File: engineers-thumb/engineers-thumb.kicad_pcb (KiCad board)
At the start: 2 copper layers, 19 parts, among them J1 Barrel_Jack_Switch, J2 AudioJack3_Switch, Q1 BC556, Q2 MMBFJ112, U1 ICL7660

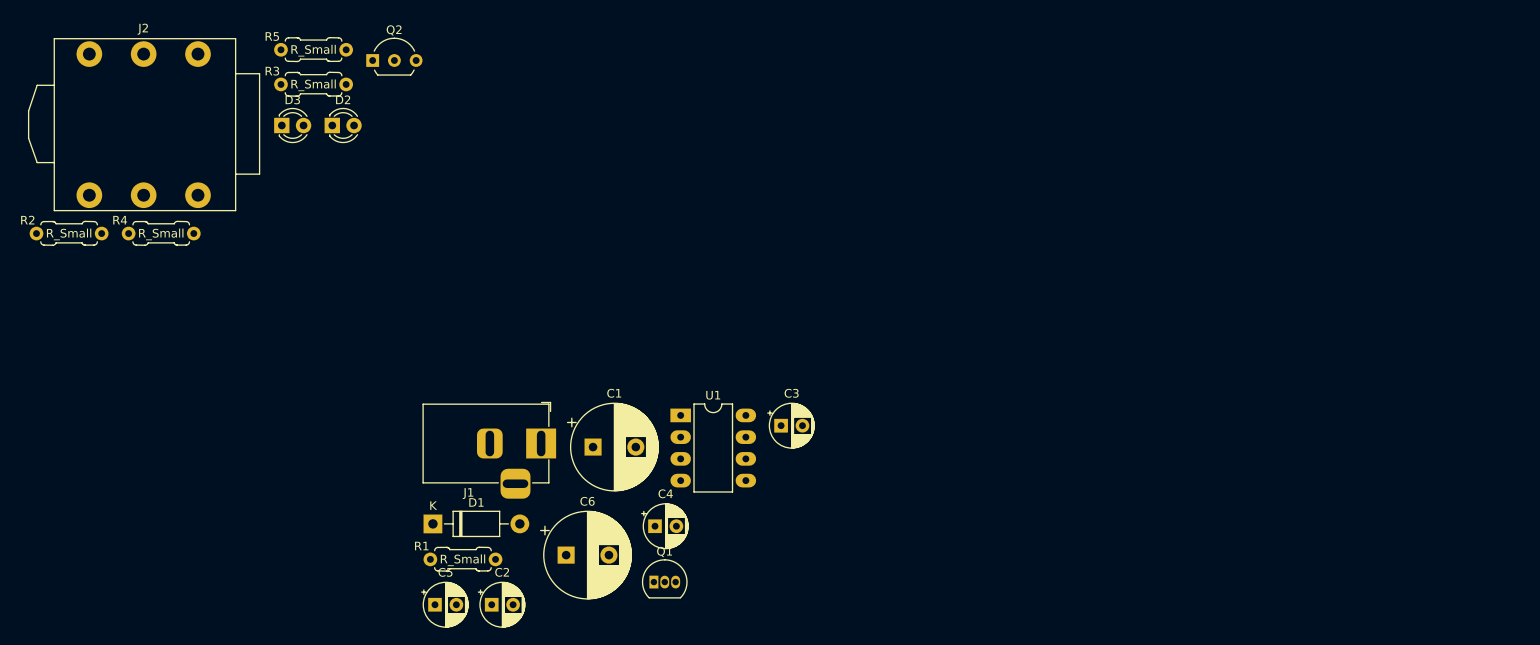
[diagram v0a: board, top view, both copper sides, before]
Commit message: Engineers Thumb 1st. cancdidate
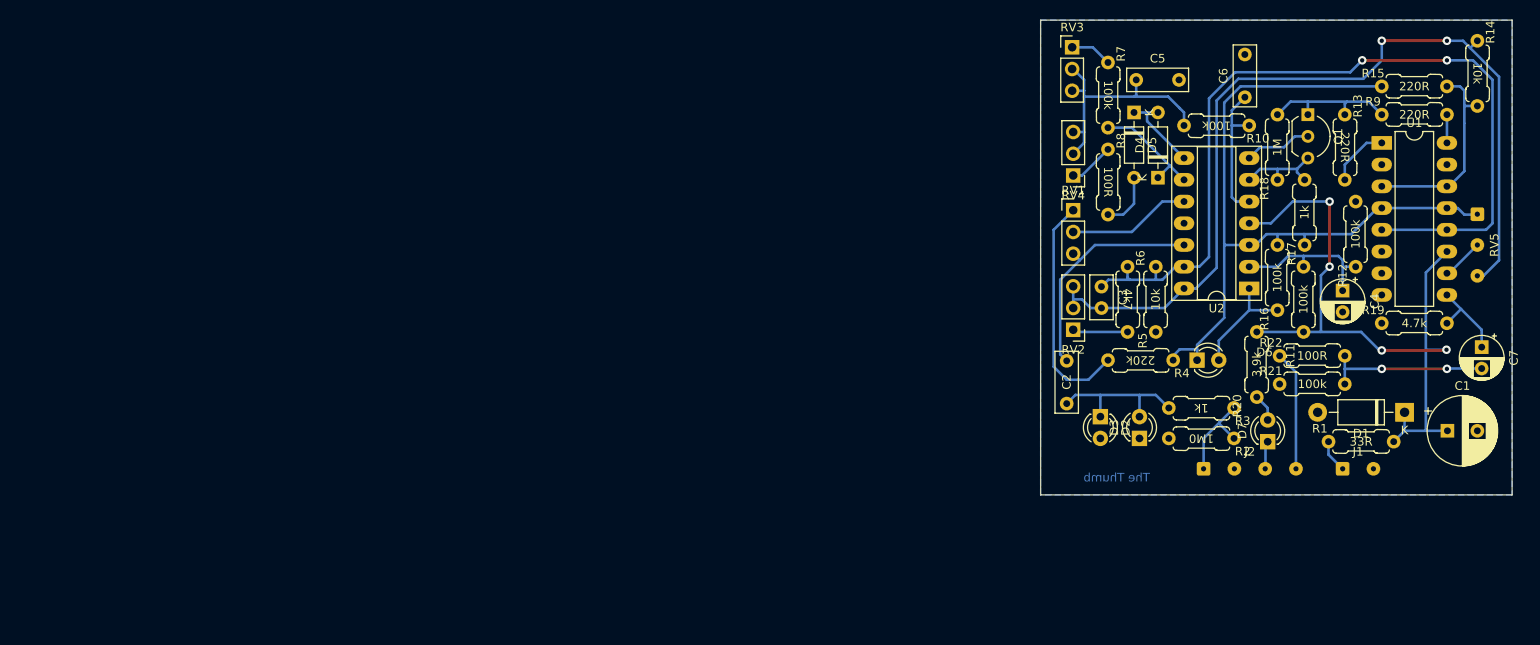
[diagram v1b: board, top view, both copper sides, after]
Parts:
- removed the C4 at (144.9, 109.1)
- removed Q2: MMBFJ112, Package_TO_SOT_THT:TO-92L_Inline_Wide
- added C2: 10n, Capacitor_THT:C_Rect_L7.0mm_W2.5mm_P5.00mm, F.Cu at (193.0, 94.7)
- added C7: 10u, Capacitor_THT:CP_Radial_D5.0mm_P2.50mm, F.Cu at (241.6, 88.1)
- added D4: 1N4148, Diode_THT:D_DO-35_SOD27_P7.62mm_Horizontal, F.Cu at (203.7, 68.3)
- added D5: 1N4148, Diode_THT:D_DO-35_SOD27_P7.62mm_Horizontal, F.Cu at (200.9, 60.7)
- added D6: LED_Small, LED_THT:LED_D3.0mm_Clear, F.Cu at (208.3, 89.7)
- added D7: LED, LED_THT:LED_D3.0mm, F.Cu at (216.5, 99.2)
- added R10: 100k, PartsStash:R_Axial_DIN0207_L6.3mm_D2.5mm_P7.62mm_Horizontal, F.Cu at (214.4, 62.2)
- added R11: 100k, PartsStash:R_Axial_DIN0207_L6.3mm_D2.5mm_P7.62mm_Horizontal, F.Cu at (220.7, 86.4)
- added R12: 100k, PartsStash:R_Axial_DIN0207_L6.3mm_D2.5mm_P7.62mm_Horizontal, F.Cu at (226.8, 78.7)
- added R13: 220R, PartsStash:R_Axial_DIN0207_L6.3mm_D2.5mm_P7.62mm_Horizontal, F.Cu at (225.6, 61.0)
- added R14: 10k, PartsStash:R_Axial_DIN0207_L6.3mm_D2.5mm_P7.62mm_Horizontal, F.Cu at (241.0, 52.3)
- added R15: 220R, PartsStash:R_Axial_DIN0207_L6.3mm_D2.5mm_P7.62mm_Horizontal, F.Cu at (229.9, 57.7)
- added R16: 100k, PartsStash:R_Axial_DIN0207_L6.3mm_D2.5mm_P7.62mm_Horizontal, F.Cu at (217.7, 83.8)
- added R17: 1k, PartsStash:R_Axial_DIN0207_L6.3mm_D2.5mm_P7.62mm_Horizontal, F.Cu at (220.9, 76.2)
- added R18: 1M, PartsStash:R_Axial_DIN0207_L6.3mm_D2.5mm_P7.62mm_Horizontal, F.Cu at (217.7, 68.6)
- added R19: 4.7k, PartsStash:R_Axial_DIN0207_L6.3mm_D2.5mm_P7.62mm_Horizontal, F.Cu at (229.9, 85.3)
- added R20: 3.9k, PartsStash:R_Axial_DIN0207_L6.3mm_D2.5mm_P7.62mm_Horizontal, F.Cu at (215.3, 94.0)
- added R21: 100k, PartsStash:R_Axial_DIN0207_L6.3mm_D2.5mm_P7.62mm_Horizontal, F.Cu at (217.9, 92.5)
- added R22: 100R, PartsStash:R_Axial_DIN0207_L6.3mm_D2.5mm_P7.62mm_Horizontal, F.Cu at (217.9, 89.2)
- added R6: 4k7, PartsStash:R_Axial_DIN0207_L6.3mm_D2.5mm_P7.62mm_Horizontal, F.Cu at (200.2, 78.7)
- added R7: 100k, PartsStash:R_Axial_DIN0207_L6.3mm_D2.5mm_P7.62mm_Horizontal, F.Cu at (197.9, 54.9)
- added R8: 100R, PartsStash:R_Axial_DIN0207_L6.3mm_D2.5mm_P7.62mm_Horizontal, F.Cu at (197.9, 65.0)
- added R9: 220R, PartsStash:R_Axial_DIN0207_L6.3mm_D2.5mm_P7.62mm_Horizontal, F.Cu at (229.9, 61.0)
- added RV1: A1M, Connector_PinHeader_2.54mm:PinHeader_1x03_P2.54mm_Vertical, F.Cu at (193.8, 72.1)
- added RV2: A1M, Connector_PinHeader_2.54mm:PinHeader_1x03_P2.54mm_Vertical, F.Cu at (193.8, 86.1)
- added RV3: A500k, Connector_PinHeader_2.54mm:PinHeader_1x03_P2.54mm_Vertical, F.Cu at (193.7, 53.1)
- added RV4: A100k, Connector_PinHeader_2.54mm:PinHeader_1x03_P2.54mm_Vertical, F.Cu at (193.8, 68.1)
- added RV5: A10k, Connector_Wire:SolderWire-0.1sqmm_1x03_P3.6mm_D0.4mm_OD1mm, F.Cu at (241.0, 72.6)
- added U2: TL074, Package_DIP:DIP-14_W7.62mm_Socket_LongPads, F.Cu at (214.4, 81.3)
- C1: value 470u -> 47u; footprint Capacitor_THT:CP_Radial_D10.0mm_P5.00mm -> Capacitor_THT:CP_Radial_D8.0mm_P3.50mm
- C3: value 10u -> 100p; footprint Capacitor_THT:CP_Radial_D5.0mm_P2.50mm -> Capacitor_THT:C_Disc_D5.0mm_W2.5mm_P2.50mm
- C5: value 10u -> 1uF; footprint Capacitor_THT:CP_Radial_D5.0mm_P2.50mm -> Capacitor_THT:C_Rect_L7.0mm_W2.5mm_P5.00mm
- C6: value 470u -> 1uF; footprint Capacitor_THT:CP_Radial_D10.0mm_P5.00mm -> Capacitor_THT:C_Rect_L7.0mm_W2.5mm_P5.00mm
- D1: value 1N5817 -> 1N4001
- D2, D3: value LED_Small -> RED
- J1: value Barrel_Jack_Switch -> power; footprint Connector_BarrelJack:BarrelJack_Horizontal -> Connector_Wire:SolderWire-0.1sqmm_1x02_P3.6mm_D0.4mm_OD1mm
- J2: value AudioJack3_Switch -> Conn_01x04_Female; footprint PartsStash:Jack_6.35mm_Rean_NYS215_Horizontal -> Connector_Wire:SolderWire-0.1sqmm_1x04_P3.6mm_D0.4mm_OD1mm
- Q1: footprint Package_TO_SOT_THT:TO-92_Inline -> Package_TO_SOT_THT:TO-92_Inline_Wide
- R1: value R_Small -> 33R
- R2: value R_Small -> 1M0
- R3: value R_Small -> 1k
- R4: value R_Small -> 220k
- R5: value R_Small -> 10k
- U1: value ICL7660 -> LM13700; footprint Package_DIP:DIP-8_W7.62mm_LongPads -> Package_DIP:DIP-16_W7.62mm_LongPads
- moved R2 142.0 mm to (212.6, 98.8), turned to 180 degrees
- moved J2 139.0 mm to (209.0, 102.4)
- moved R4 123.0 mm to (205.5, 89.7), turned to 180 degrees
- moved R3 117.7 mm to (212.6, 95.2), turned to 180 degrees
- moved D1 114.3 mm to (232.5, 95.8), turned to 180 degrees
- moved R5 107.5 mm to (203.5, 86.4), turned to 90 degrees
- moved D3 106.7 mm to (201.5, 98.8), turned to 90 degrees
- moved C4 106.0 mm to (225.3, 81.5), turned to -90 degrees
- moved R1 105.9 mm to (223.6, 99.2)
- moved C5 102.4 mm to (201.2, 56.9)
- moved C1 99.9 mm to (237.5, 97.9)
- moved D2 96.0 mm to (197.0, 96.3), turned to -90 degrees
- moved C6 95.7 mm to (213.9, 58.9), turned to 90 degrees
- moved Q1 94.0 mm to (221.2, 61.0), turned to -90 degrees
- moved J1 93.7 mm to (225.3, 102.4)
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- renumbered C2 to C4
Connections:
- C3 pad 1: Net-(C3-Pad1) -> /fb_return
- C3 pad 2: Net-(C3-Pad2) -> /amplified
- C4 pad 1: +9V -> Net-(C4-Pad1)
- C6 pad 1: -8V -> Net-(C6-Pad1)
- D1 pad 2: Net-(D1-Pad2) -> GND
- J1 pad 1: GND -> PWR
- J1 pad 2: Net-(D1-Pad2) -> GND
- Q1 pad 1: Net-(C4-Pad1) -> Net-(Q1-Pad1)
- Q1 pad 2: Net-(C5-Pad1) -> Net-(Q1-Pad2)
- Q1 pad 3: -8V -> Net-(Q1-Pad3)
- R1 pad 1: Net-(C4-Pad1) -> PWR
- R1 pad 2: Net-(C5-Pad1) -> +9V
- R2 pad 1: Net-(J2-PadT) -> INPUT
- R3 pad 1: Net-(J2-PadT) -> INPUT
- R4 pad 1: +9V -> +4.5V
- R5 pad 1: Net-(Q2-Pad2) -> GND
- R5 pad 2: GND -> /fb_return
- U1 pad 1: unconnected-(U1-Pad1) -> Net-(R13-Pad2)
- U1 pad 2: Net-(C3-Pad1) -> unconnected-(U1-Pad2)
- U1 pad 3: GND -> /fb_send
- U1 pad 4: Net-(C3-Pad2) -> +4.5V
- U1 pad 5: Net-(C4-Pad1) -> /fb_return
- U1 pad 6: unconnected-(U1-Pad6) -> GND
- U1 pad 8: +9V -> unconnected-(U1-Pad8)
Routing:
- net /amplified: track 0.00 -> 106.1 mm, vias 0 -> 2
- net /fb_return: track 0.00 -> 101.7 mm, vias 0 -> 2
- net +4.5V: track 0.00 -> 88.4 mm
- net +9V: track 0.00 -> 82.6 mm, vias 0 -> 4
- net Net-(C5-Pad1): track 0.00 -> 29.5 mm
- net Net-(R4-Pad2): track 0.00 -> 27.2 mm
- net Net-(C2-Pad2): track 0.00 -> 27.0 mm
- net /fb_send: track 0.00 -> 23.6 mm
- net Net-(C7-Pad2): track 0.00 -> 19.3 mm, vias 0 -> 2
- net Net-(C2-Pad1): track 0.00 -> 18.1 mm
- net Net-(C4-Pad1): track 0.00 -> 18.0 mm
- net Net-(Q1-Pad1): track 0.00 -> 16.6 mm
- net Net-(C6-Pad1): track 0.00 -> 16.6 mm
- net Net-(RV1-Pad2): track 0.00 -> 14.4 mm
- net OUTPUT: track 0.00 -> 14.0 mm
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- added copper zone on B.Cu, net GND
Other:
- board outline added: 55.1 x 55.5 mm
- board text added: "The Thumb"

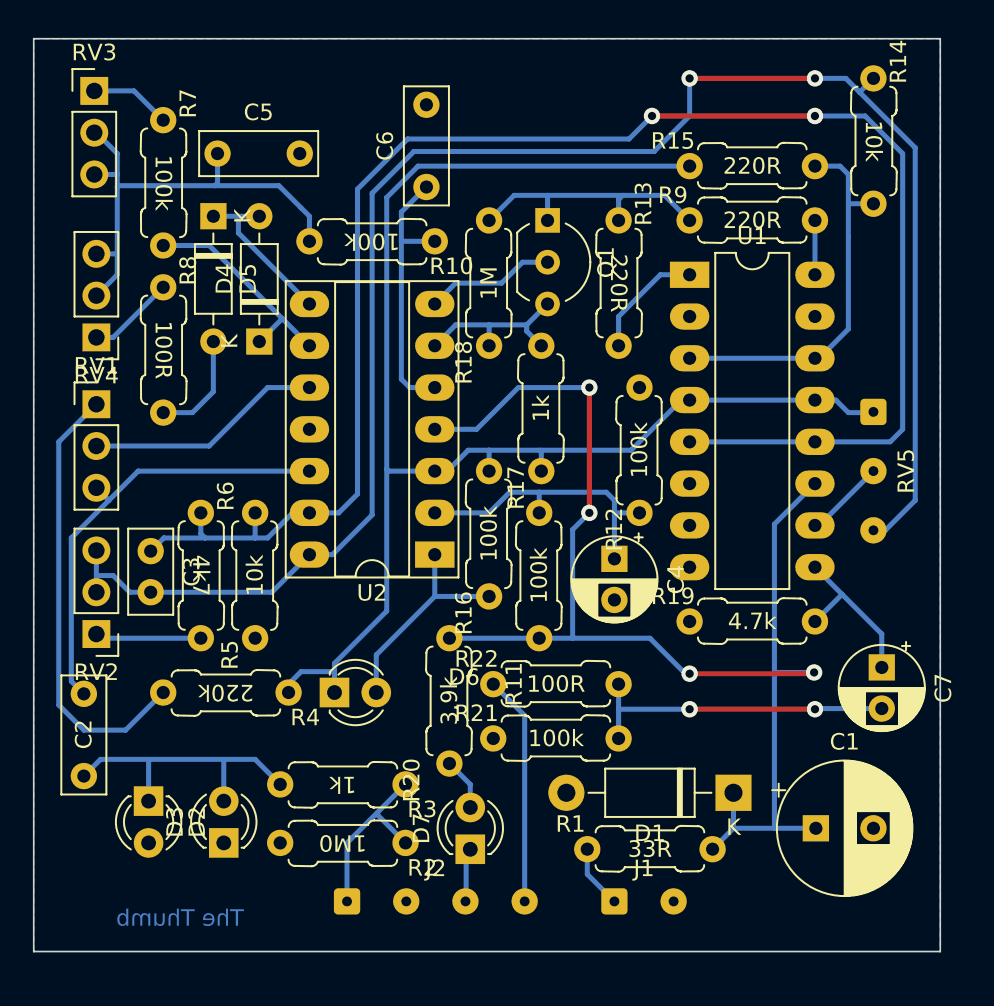
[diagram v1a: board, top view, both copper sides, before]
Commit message: Resized vias.
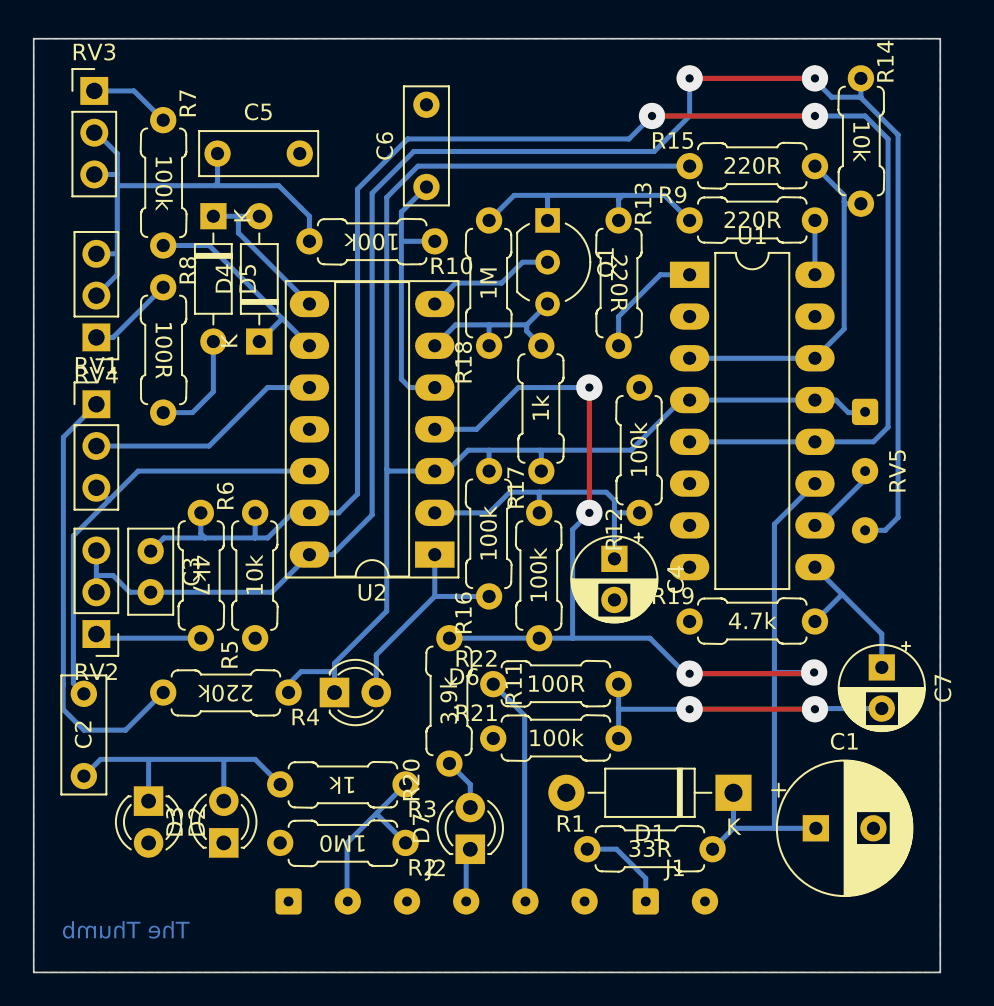
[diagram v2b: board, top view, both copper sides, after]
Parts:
- J2: value Conn_01x04_Female -> Conn_01x06_Female; footprint Connector_Wire:SolderWire-0.1sqmm_1x04_P3.6mm_D0.4mm_OD1mm -> Connector_Wire:SolderWire-0.1sqmm_1x06_P3.6mm_D0.4mm_OD1mm
- moved J2 3.56 mm to (205.5, 102.4)
- moved J1 1.91 mm to (227.2, 102.4)
- moved R14 0.76 mm to (240.3, 52.3)
- moved RV5 0.51 mm to (240.5, 72.6)
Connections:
- J2 pad 1: INPUT -> GND
- J2 pad 2: GND -> INPUT
- J2 pad 3: SWITCH -> GND
- J2 pad 4: OUTPUT -> SWITCH
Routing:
- net PWR: track 3.86 -> 5.69 mm
- net /fb_send: track 23.6 -> 21.8 mm
- net /fb_return: track 101.7 -> 100.3 mm
- net +4.5V: track 88.4 -> 87.9 mm
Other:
- board size 55.1 x 55.5 mm -> 55.1 x 56.8 mm
